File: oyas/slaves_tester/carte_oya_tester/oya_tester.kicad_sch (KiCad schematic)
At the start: 32 parts, among them J1 Conn_01x02, J2 Conn_01x04, U1 D148K, U2 MAX485E, U3 BPC_Alim5V

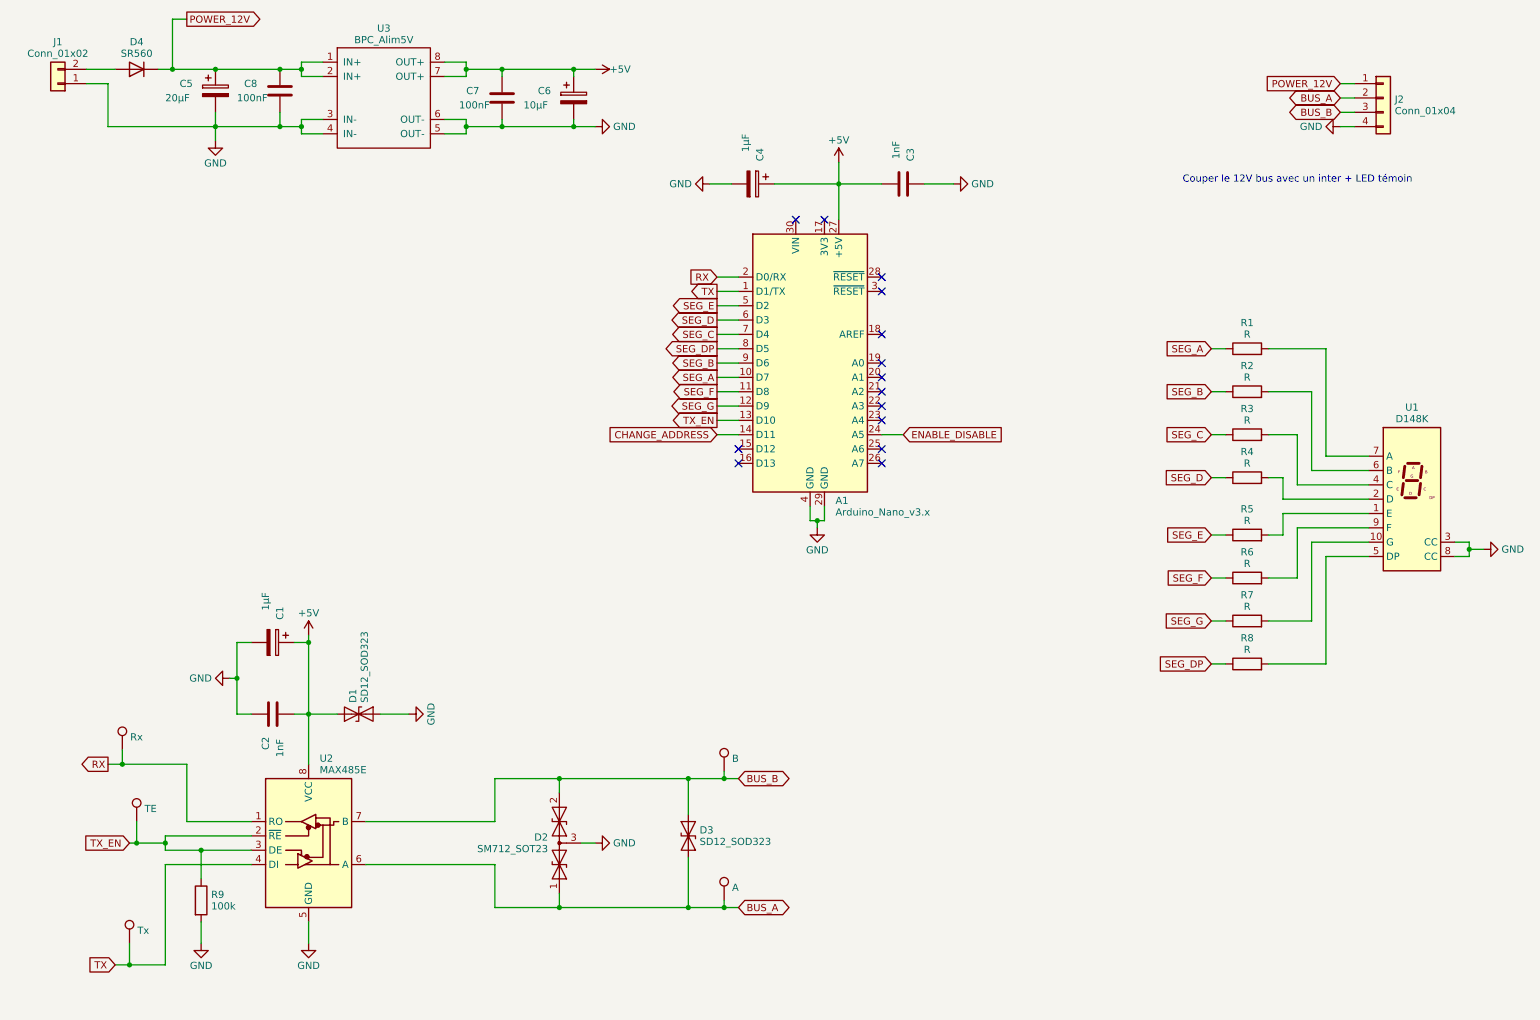
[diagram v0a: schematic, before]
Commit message: Changement forme de la carte (boîte de dérivation)
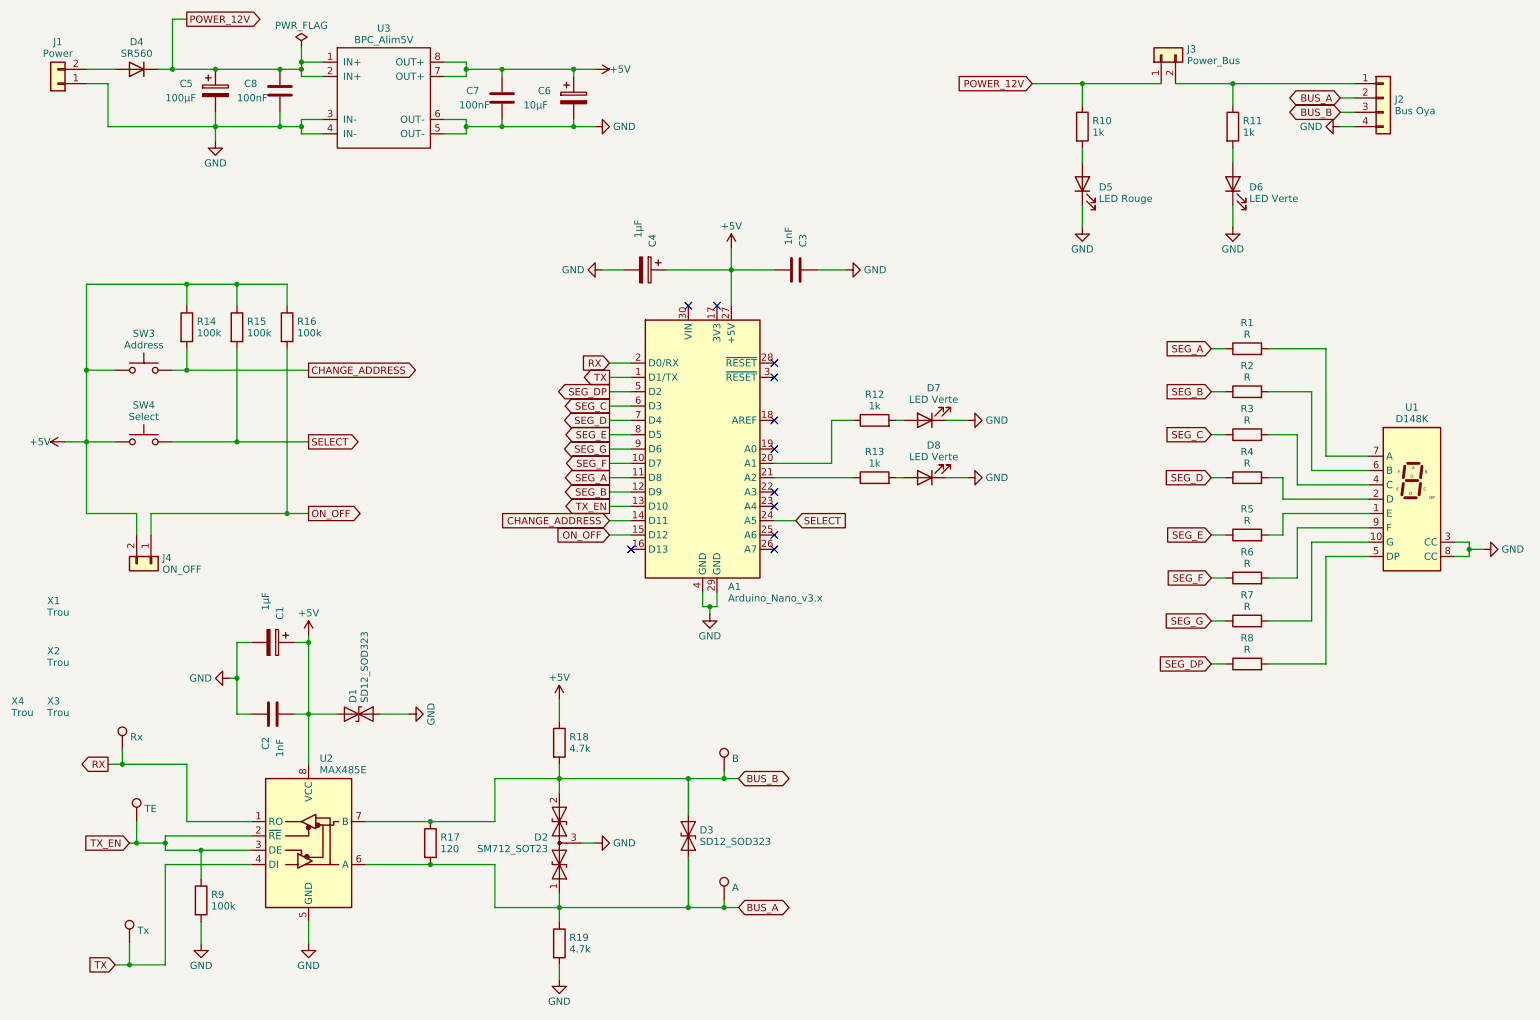
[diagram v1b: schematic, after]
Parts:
- removed U1: D148K, Display_7Segment:D1X8K, symbol Display_Character:D148K
- added D5: LED Rouge, LED_THT:LED_D3.0mm_FlatTop, symbol Device:LED
- added D6, D7, D8: LED Verte, LED_THT:LED_D3.0mm_FlatTop, symbol Device:LED
- added J3: Power_Bus, Connector_PinHeader_2.54mm:PinHeader_1x02_P2.54mm_Vertical, symbol Connector_Generic:Conn_01x02
- added J4: ON_OFF, Connector_PinHeader_2.54mm:PinHeader_1x02_P2.54mm_Vertical, symbol Connector_Generic:Conn_01x02
- added R10, R11, R12, R13: 1k, Resistor_SMD:R_0805_2012Metric_Pad1.20x1.40mm_HandSolder, symbol Device:R
- added R14, R15, R16: 100k, Resistor_SMD:R_0805_2012Metric_Pad1.20x1.40mm_HandSolder, symbol Device:R
- added R17: 120, Resistor_THT:R_Axial_DIN0204_L3.6mm_D1.6mm_P5.08mm_Horizontal, symbol Device:R
- added R18, R19: 4.7k, Resistor_THT:R_Axial_DIN0204_L3.6mm_D1.6mm_P5.08mm_Horizontal, symbol Device:R
- added SW3: Address, Button_Switch_THT:SW_PUSH_6mm, symbol Switch:SW_Push
- added SW4: Select, Button_Switch_THT:SW_PUSH_6mm, symbol Switch:SW_Push
- added U1: D148K, bpc:BPC_7SEG_D1X8K, symbol bpc:BPC_7SEG_D148K
- added X1, X2, X3, X4: Trou, bpc:BPC_Trou4mm_Fixation, symbol bpc:BPC_TROU
- C5: value 20µF -> 100µF; footprint Capacitor_SMD:C_0805_2012Metric_Pad1.18x1.45mm_HandSolder -> Capacitor_THT:CP_Radial_D8.0mm_P3.50mm
- C6: footprint Capacitor_SMD:C_0805_2012Metric_Pad1.18x1.45mm_HandSolder -> Capacitor_THT:CP_Radial_D5.0mm_P2.50mm
- J1: value Conn_01x02 -> Power; footprint (none) -> TerminalBlock_Phoenix:TerminalBlock_Phoenix_MKDS-1,5-2-5.08_1x02_P5.08mm_Horizontal
- J2: value Conn_01x04 -> Bus Oya; footprint (none) -> TerminalBlock_Phoenix:TerminalBlock_Phoenix_MKDS-1,5-4-5.08_1x04_P5.08mm_Horizontal
- R1, R2, R3, R4, R5, R6, R7, R8: footprint (none) -> Resistor_SMD:R_0805_2012Metric_Pad1.20x1.40mm_HandSolder
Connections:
- net +5V: now also J4.2 (Pin_2), R14.1, R15.1, R16.1, R18.1, SW3.1, SW4.1
- net BUS_A: now also R17.2, R19.1
- net BUS_B: now also R17.1, R18.2
- net CHANGE_ADDRESS: now also R14.2, SW3.2
- net GND: now also D5.1 (K), D6.1 (K), D7.1 (K), D8.1 (K), R19.2, U1.3 (CC), U1.8 (CC)
- net POWER_12V: now also J3.1 (Pin_1), R10.1; no longer J2.1 (Pin_1)
- net SEG_A: now also A1.11 (D8); no longer A1.10 (D7)
- net SEG_B: now also A1.12 (D9); no longer A1.9 (D6)
- net SEG_C: now also A1.6 (D3); no longer A1.7 (D4)
- net SEG_D: now also A1.7 (D4); no longer A1.6 (D3)
- net SEG_DP: now also A1.5 (D2); no longer A1.8 (D5)
- net SEG_E: now also A1.8 (D5); no longer A1.5 (D2)
- net SEG_F: now also A1.10 (D7); no longer A1.11 (D8)
- net SEG_G: now also A1.9 (D6); no longer A1.12 (D9)
- net at R6.2: now also U1.9 (F)
- net at R3.2: now also U1.4 (C)
- net at R8.2: now also U1.5 (DP)
- net at R7.2: now also U1.10 (G)
- net at R4.2: now also U1.2 (D)
- net at R5.2: now also U1.1 (E)
- net at R2.2: now also U1.6 (B)
- net at R1.2: now also U1.7 (A)
- net ON_OFF: now reaches A1.15 (D12)
- net ON_OFF: now also J4.1 (Pin_1), R16.2
- net at A1.20 (A1): now also R12.1
- net at A1.21 (A2): now also R13.1
- net ENABLE_DISABLE renamed SELECT
- net SELECT: now also R15.2, SW4.2
- new net: J2.1 (Pin_1), J3.2 (Pin_2), R11.1
- new net: D8.2 (A), R13.2
- new net: D6.2 (A), R11.2
- new net: D7.2 (A), R12.2
- new net: D5.2 (A), R10.2
- no-connect marks 14 -> 11
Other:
- note removed: "Couper le 12V bus avec un inter + LED témoin"
- company: (none) -> BPC
- title: (none) -> Carte testeur d'Oya
- moved on the sheet: A1, C3, C4

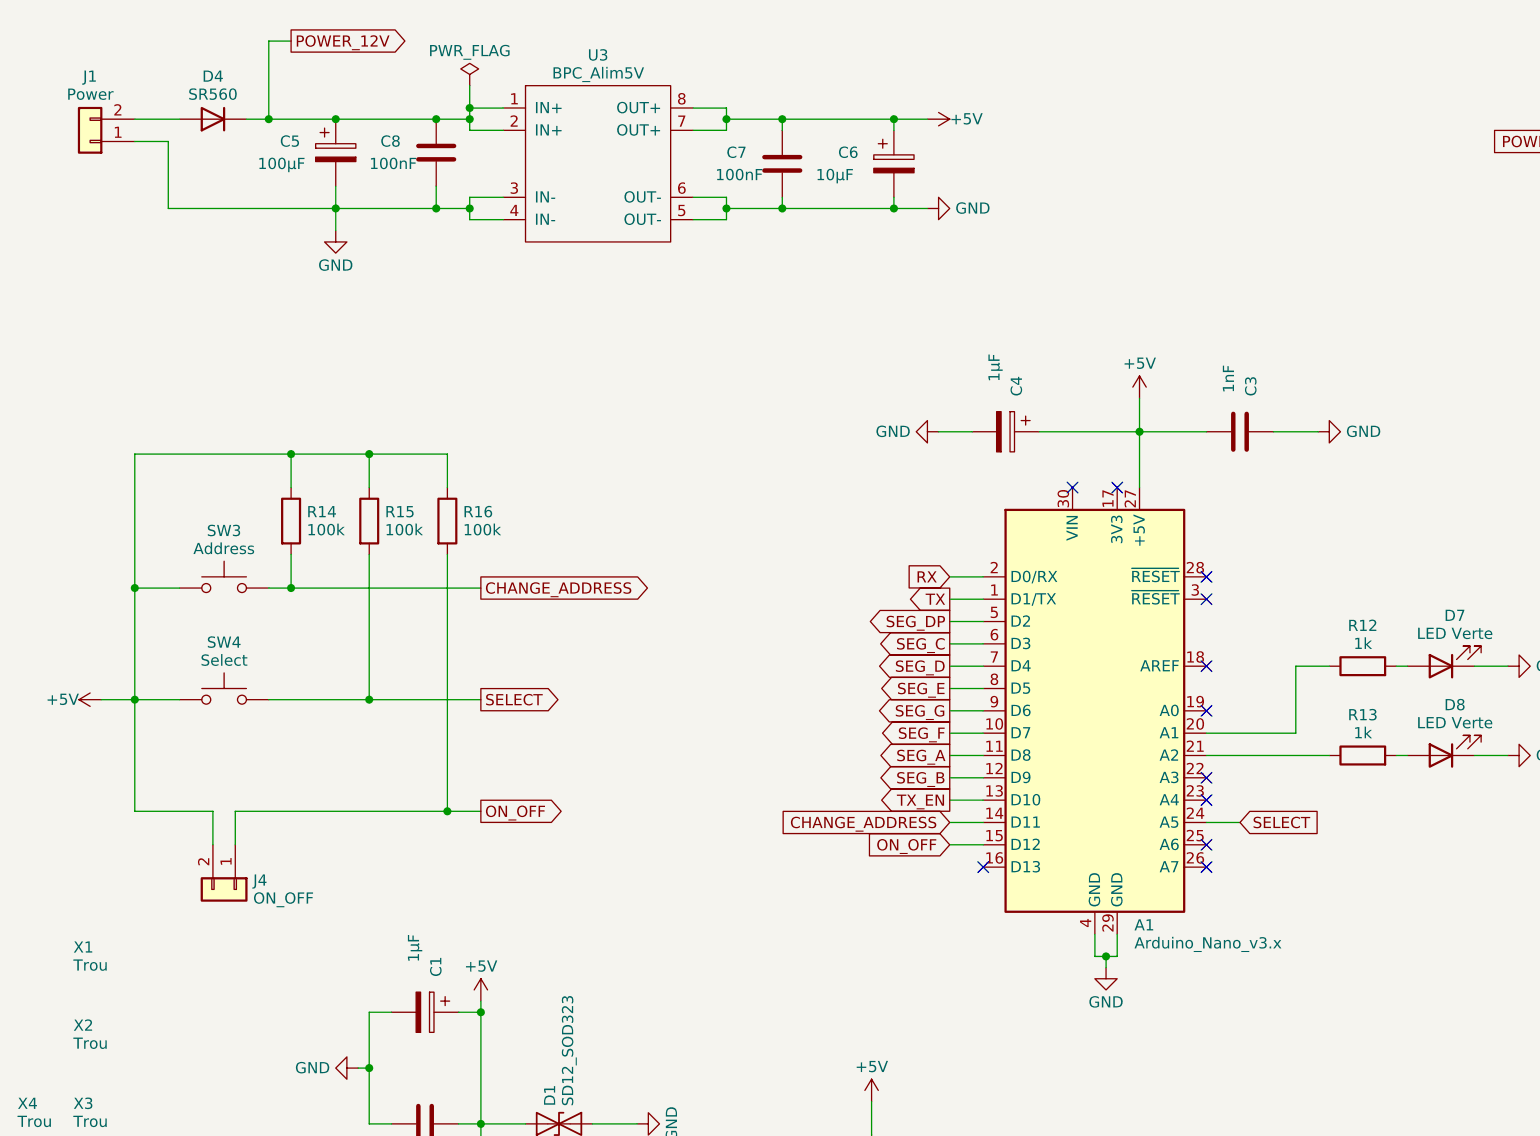
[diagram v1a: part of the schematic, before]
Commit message: Finalisation testeur Connecteurs des interrupteurs à choisir...
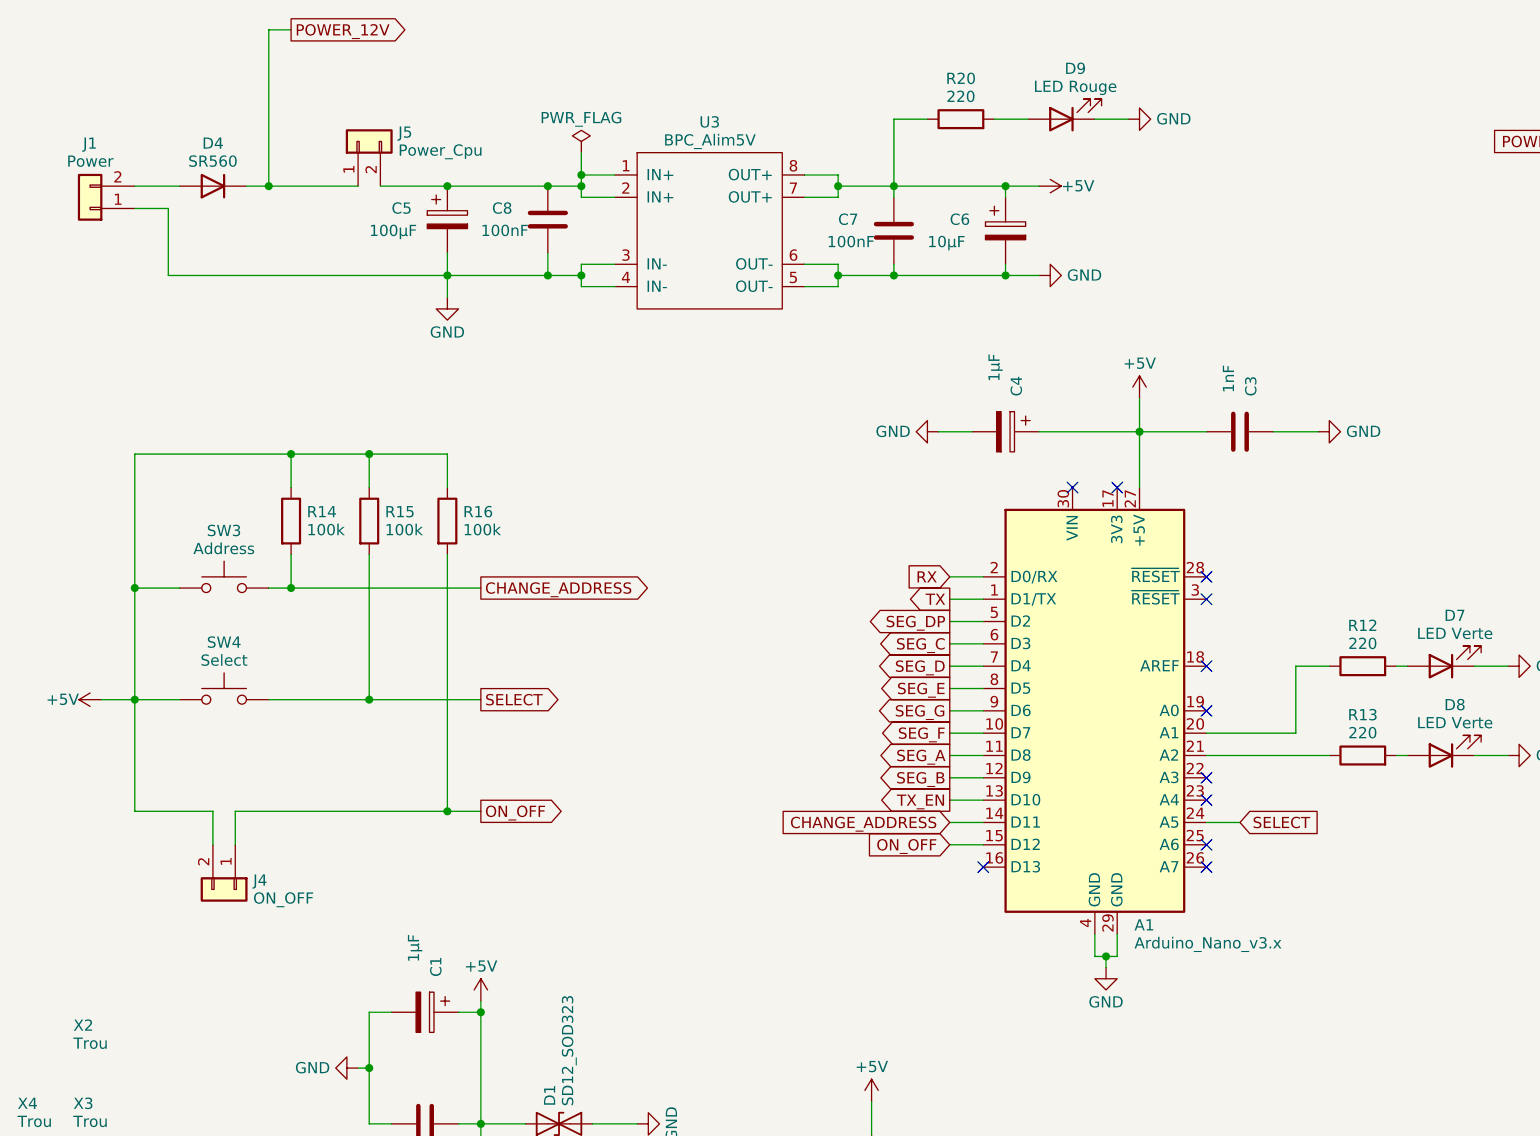
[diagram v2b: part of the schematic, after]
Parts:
- removed X1: Trou, bpc:BPC_Trou4mm_Fixation, symbol bpc:BPC_TROU
- added D9: LED Rouge, LED_THT:LED_D3.0mm_FlatTop, symbol Device:LED
- added J5: Power_Cpu, Connector_PinHeader_2.54mm:PinHeader_1x02_P2.54mm_Vertical, symbol Connector_Generic:Conn_01x02
- added R20: 220, Resistor_SMD:R_0805_2012Metric_Pad1.20x1.40mm_HandSolder, symbol Device:R
- R12, R13: value 1k -> 220
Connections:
- net +5V: now also R20.1
- net GND: now also D9.1 (K)
- net POWER_12V: now also J5.1 (Pin_1); no longer C5.1, C8.1, U3.1 (IN+), U3.2 (IN+)
- new net: C5.1, C8.1, J5.2 (Pin_2), U3.1 (IN+), U3.2 (IN+)
- new net: D9.2 (A), R20.2
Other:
- moved on the sheet: C5, C6, C7, C8, D4, J1, U3

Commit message: Finition
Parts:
- removed J3: Power_Bus, Connector_PinHeader_2.54mm:PinHeader_1x02_P2.54mm_Vertical, symbol Connector_Generic:Conn_01x02
- removed J4: ON_OFF, Connector_PinHeader_2.54mm:PinHeader_1x02_P2.54mm_Vertical, symbol Connector_Generic:Conn_01x02
- removed J5: Power_Cpu, Connector_PinHeader_2.54mm:PinHeader_1x02_P2.54mm_Vertical, symbol Connector_Generic:Conn_01x02
- added C9: 1000µF, Capacitor_THT:CP_Radial_D16.0mm_P7.50mm, symbol Device:C_Polarized
- added J6: Switches, Connector_JST:JST_VH_B6P-VH-FB-B_1x06_P3.96mm_Vertical, symbol Connector_Generic:Conn_01x06
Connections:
- net +5V: now also J6.5 (Pin_5)
- net GND: now also C9.2
- net ON_OFF: now also J6.6 (Pin_6)
- net POWER_12V: now also J6.1 (Pin_1), J6.3 (Pin_3)
- net SW_BUS_2: now reaches J2.1 (Pin_1), R11.1
- net SW_BUS_2: now also C9.1, J6.2 (Pin_2)
- net SW_CPU_2: now reaches C5.1, C8.1, U3.1 (IN+), U3.2 (IN+)
- net SW_CPU_2: now also J6.4 (Pin_4)
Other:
- note added: "Non montés"
- moved on the sheet: D6, J2, R11
